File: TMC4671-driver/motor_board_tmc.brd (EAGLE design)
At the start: 60 x 110 mm, 163 parts, among them U1 TMC4671, U10 BSC030N08NS5ATMA1, U11 BSC030N08NS5ATMA1, U12 BSC030N08NS5ATMA1, U13 BSC030N08NS5ATMA1, U14 MCP14XX, U15 BSC030N08NS5ATMA1, U16 BSC030N08NS5ATMA1, U17 BSC030N08NS5ATMA1, U18 NC7NZ17K8X-3-BUFFER, U19 NC7NZ17K8X-3-BUFFER, U2 LM5109BSD, U20 LM74700-Q1, U22 BSC030N08NS5ATMA1, U23 MAX5033BASA+T, U24 AP3012KTR-G1, U3 LM5109BSD, U4 LM5109BSD, U5 LM5109BSD, U6 BSC030N08NS5ATMA1, U7 BSC030N08NS5ATMA1, U8 AD841X, U9 AD841X, X1 2516-, X2 GMSTBA4, X3 GMSTBA4, Y1 25MHz

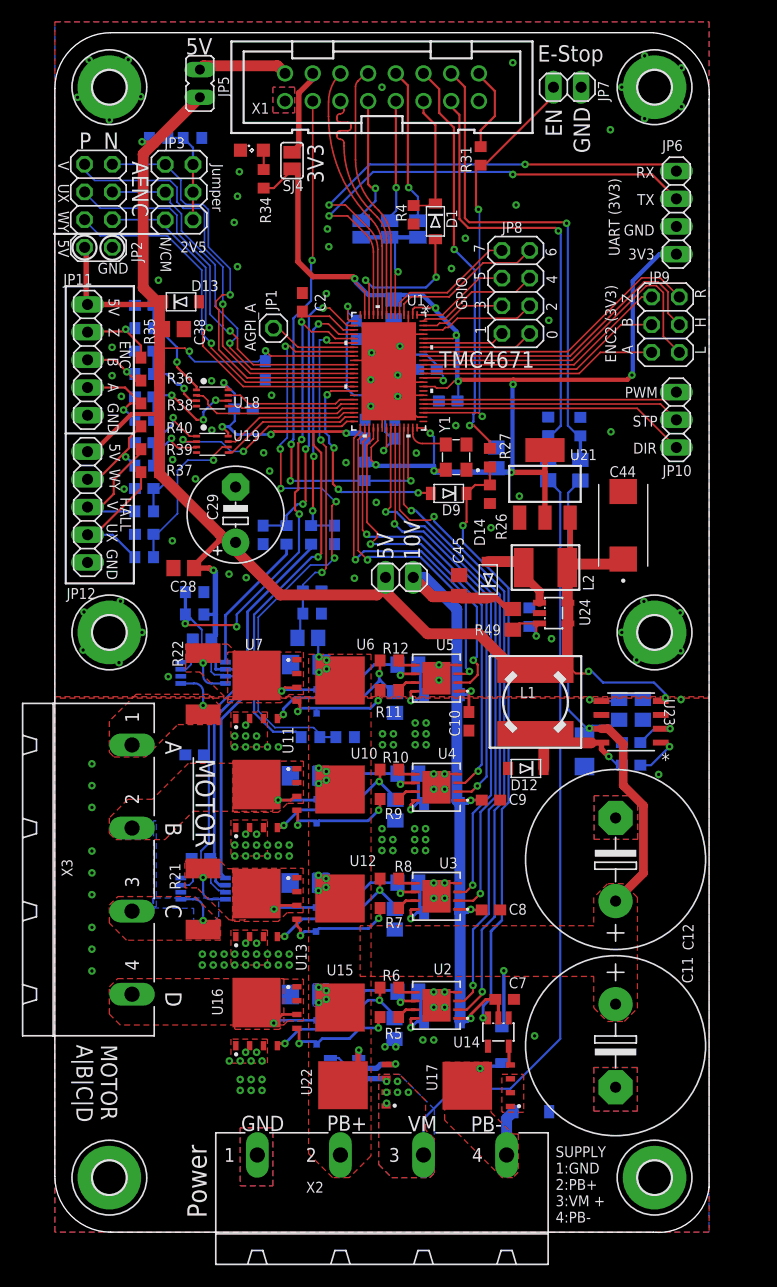
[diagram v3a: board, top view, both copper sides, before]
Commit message: Added E-Stop cap
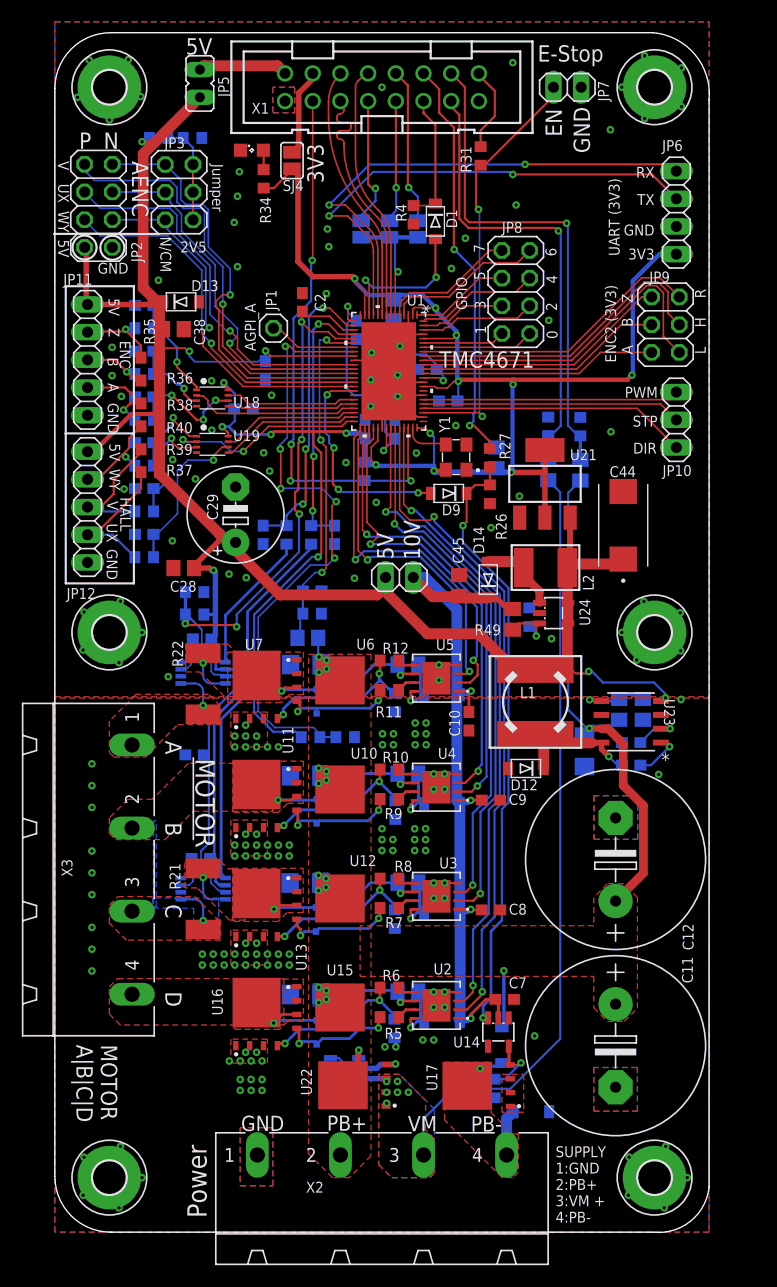
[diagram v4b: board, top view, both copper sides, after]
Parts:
- added R51: 33k, resistor:R0603
- C45: value 4.7µF -> 4.7µF <REMOVE>
- R17, R20, R25, R28: device resistor:R0805 -> resistor:R0603
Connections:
- net BRAKE_GATE: now also R51.2
- net GND: now also R51.1
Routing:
- net BRAKE_GATE: track 1.78 -> 5.88 mm, vias 0 -> 1
- net GND: vias 171 -> 181
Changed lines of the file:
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@@
 </element>
 <element name="D14" library="adafruit" library_urn="urn:adsk.eagle:library:420" package="SOD-123FL" package3d_urn="urn:adsk.eagle:package:6240937/1" value="LV low drop" x="39.75" y="-50.15" locked="yes" smashed="yes" rot="R90">
-<attribute name="NAME" x="39.45" y="-47.075" size="1" layer="25" font="vector" rot="R90"/>
+<attribute name="NAME" x="39.375" y="-47.8" size="1" layer="25" font="vector" rot="R90"/>
 <attribute name="VALUE" x="42.05" y="-51.25" size="1.27" layer="27" rot="R90"/>
 </element>
@@
 <attribute name="VALUE" x="45.43" y="-51.965" size="1" layer="28" rot="MR270"/>
 </element>
-<element name="C45" library="resistor" library_urn="urn:adsk.eagle:library:348" package="C0805" package3d_urn="urn:adsk.eagle:package:23617/2" value="4.7µF" x="37.075" y="-50.7" locked="yes" smashed="yes" rot="R90">
+<element name="C45" library="resistor" library_urn="urn:adsk.eagle:library:348" package="C0805" package3d_urn="urn:adsk.eagle:package:23617/2" value="4.7µF &lt;REMOVE&gt;" x="37.075" y="-50.7" locked="yes" smashed="yes" rot="R90">
 <attribute name="NAME" x="37.49" y="-48.685" size="1" layer="25" font="vector" rot="R90"/>
 <attribute name="VALUE" x="38.98" y="-51.335" size="1.27" layer="27" rot="R90"/>
@@
 <attribute name="VALUE" x="21.7" y="-92.775" size="1.27" layer="28" rot="MR90"/>
 </element>
-<element name="R17" library="resistor" library_urn="urn:adsk.eagle:library:348" package="R0805" package3d_urn="urn:adsk.eagle:package:23553/2" value="33k" x="31.2" y="-61.425" locked="yes" smashed="yes" rot="MR90">
+<element name="R17" library="resistor" library_urn="urn:adsk.eagle:library:348" package="R0603" package3d_urn="urn:adsk.eagle:package:23555/3" value="33k" x="31.2" y="-61.425" locked="yes" smashed="yes" rot="MR90">
 <attribute name="NAME" x="30.11" y="-60.58" size="1" layer="26" font="vector" rot="MR0"/>
 <attribute name="VALUE" x="28.66" y="-62.06" size="1.27" layer="28" rot="MR90"/>
 </element>
-<element name="R20" library="resistor" library_urn="urn:adsk.eagle:library:348" package="R0805" package3d_urn="urn:adsk.eagle:package:23553/2" value="33k" x="31.225" y="-71.3" locked="yes" smashed="yes" rot="MR90">
+<element name="R20" library="resistor" library_urn="urn:adsk.eagle:library:348" package="R0603" package3d_urn="urn:adsk.eagle:package:23555/3" value="33k" x="31.225" y="-71.3" locked="yes" smashed="yes" rot="MR90">
 <attribute name="NAME" x="30.285" y="-70.78" size="1" layer="26" font="vector" rot="MR0"/>
 <attribute name="VALUE" x="28.685" y="-71.935" size="1.27" layer="28" rot="MR90"/>
 </element>
-<element name="R25" library="resistor" library_urn="urn:adsk.eagle:library:348" package="R0805" package3d_urn="urn:adsk.eagle:package:23553/2" value="33k" x="31.175" y="-81.3" locked="yes" smashed="yes" rot="MR90">
+<element name="R25" library="resistor" library_urn="urn:adsk.eagle:library:348" package="R0603" package3d_urn="urn:adsk.eagle:package:23555/3" value="33k" x="31.175" y="-81.3" locked="yes" smashed="yes" rot="MR90">
 <attribute name="NAME" x="33.205" y="-82.04" size="1" layer="26" font="vector" rot="MR270"/>
 <attribute name="VALUE" x="28.635" y="-81.935" size="1.27" layer="28" rot="MR90"/>
 </element>
-<element name="R28" library="resistor" library_urn="urn:adsk.eagle:library:348" package="R0805" package3d_urn="urn:adsk.eagle:package:23553/2" value="33k" x="31.15" y="-91.325" locked="yes" smashed="yes" rot="MR90">
+<element name="R28" library="resistor" library_urn="urn:adsk.eagle:library:348" package="R0603" package3d_urn="urn:adsk.eagle:package:23555/3" value="33k" x="31.15" y="-91.325" locked="yes" smashed="yes" rot="MR90">
 <attribute name="NAME" x="33.005" y="-91.915" size="1" layer="26" font="vector" rot="MR270"/>
 <attribute name="VALUE" x="28.61" y="-91.96" size="1.27" layer="28" rot="MR90"/>
@@
 <attribute name="NAME" x="45.2" y="-97.825" size="1" layer="26" rot="MR0"/>
 <attribute name="VALUE" x="42.6" y="-97.666" size="0.4064" layer="28" rot="MR180"/>
+</element>
+<element name="R51" library="resistor" library_urn="urn:adsk.eagle:library:348" package="R0603" package3d_urn="urn:adsk.eagle:package:23555/3" value="33k" x="40.325" y="-96.825" smashed="yes" rot="MR90">
+<attribute name="NAME" x="41.595" y="-97.46" size="1.27" layer="26" rot="MR90"/>
+<attribute name="VALUE" x="37.785" y="-97.46" size="1.27" layer="28" rot="MR90"/>
 </element>
 </elements>
@@
 <via x="44" y="-92" extent="1-16" drill="0.3"/>
 <contactref element="D15" pad="A"/>
+<contactref element="R51" pad="1"/>
+<via x="58" y="-105" extent="1-16" drill="0.3"/>
+<via x="55.88375625" y="-107.772421875" extent="1-16" drill="0.3"/>
+<via x="52.593071875" y="-106.616484375" extent="1-16" drill="0.3"/>
+<via x="52.67555625" y="-103.12965" extent="1-16" drill="0.3"/>
+<via x="56.017221875" y="-102.13060625" extent="1-16" drill="0.3"/>
+<via x="8" y="-105" extent="1-16" drill="0.3"/>
+<via x="5.88375625" y="-107.772421875" extent="1-16" drill="0.3"/>
+<via x="2.593071875" y="-106.616484375" extent="1-16" drill="0.3"/>
+<via x="2.67555625" y="-103.12965" extent="1-16" drill="0.3"/>
+<via x="6.017221875" y="-102.13060625" extent="1-16" drill="0.3"/>
 </signal>
 <signal name="G_LS_D">
@@
 <wire x1="31.15" y1="-90.375" x2="31.15" y2="-90.1084" width="0.254" layer="16"/>
 <wire x1="31.15" y1="-90.1084" x2="29.775" y2="-88.7334" width="0.254" layer="16"/>
+<wire x1="31.15" y1="-90.375" x2="31.15" y2="-90.475" width="0" layer="19" extent="16-16"/>
 </signal>
 <signal name="MOT_C">
@@
 <wire x1="31.175" y1="-80.35" x2="31.175" y2="-80.0084" width="0.254" layer="16"/>
 <wire x1="31.175" y1="-80.0084" x2="29.8" y2="-78.6334" width="0.254" layer="16"/>
+<wire x1="31.175" y1="-80.35" x2="31.175" y2="-80.45" width="0" layer="19" extent="16-16"/>
 </signal>
 <signal name="G_HS_C">
@@
 <wire x1="31.2" y1="-60.475" x2="30.925" y2="-60.475" width="0.254" layer="16"/>
 <wire x1="30.925" y1="-60.475" x2="29.825" y2="-59.375" width="0.254" layer="16"/>
+<wire x1="31.2" y1="-60.475" x2="31.2" y2="-60.575" width="0" layer="19" extent="16-16"/>
 </signal>
 <signal name="G_LS_B">
@@
 <wire x1="29.75" y1="-68.675" x2="31.225" y2="-70.15" width="0.254" layer="16"/>
 <wire x1="31.225" y1="-70.15" x2="31.225" y2="-70.35" width="0.254" layer="16"/>
+<wire x1="31.225" y1="-70.35" x2="31.225" y2="-70.45" width="0" layer="19" extent="16-16"/>
 </signal>
 <signal name="INPUT_GATE">
@@
 <wire x1="41.775" y1="-94.67" x2="41.65" y2="-94.545" width="0.3" layer="1"/>
 <wire x1="41.625" y1="-92.95" x2="41.65" y2="-92.975" width="0.3" layer="1"/>
+<contactref element="R51" pad="2"/>
+<wire x1="40.325" y1="-95.975" x2="41.25" y2="-95.975" width="0.2" layer="16"/>
+<wire x1="41.25" y1="-95.975" x2="42.75" y2="-94.475" width="0.2" layer="16"/>
+<via x="42.75" y="-94.475" extent="1-16" drill="0.3"/>
+<wire x1="42.75" y1="-94.475" x2="42.555" y2="-94.67" width="0.2" layer="1"/>
+<wire x1="42.555" y1="-94.67" x2="41.775" y2="-94.67" width="0.2" layer="1"/>
 </signal>
 <signal name="V_SENSE/2">

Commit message: Fixed tmc silkscreen (Resistor names, labels)
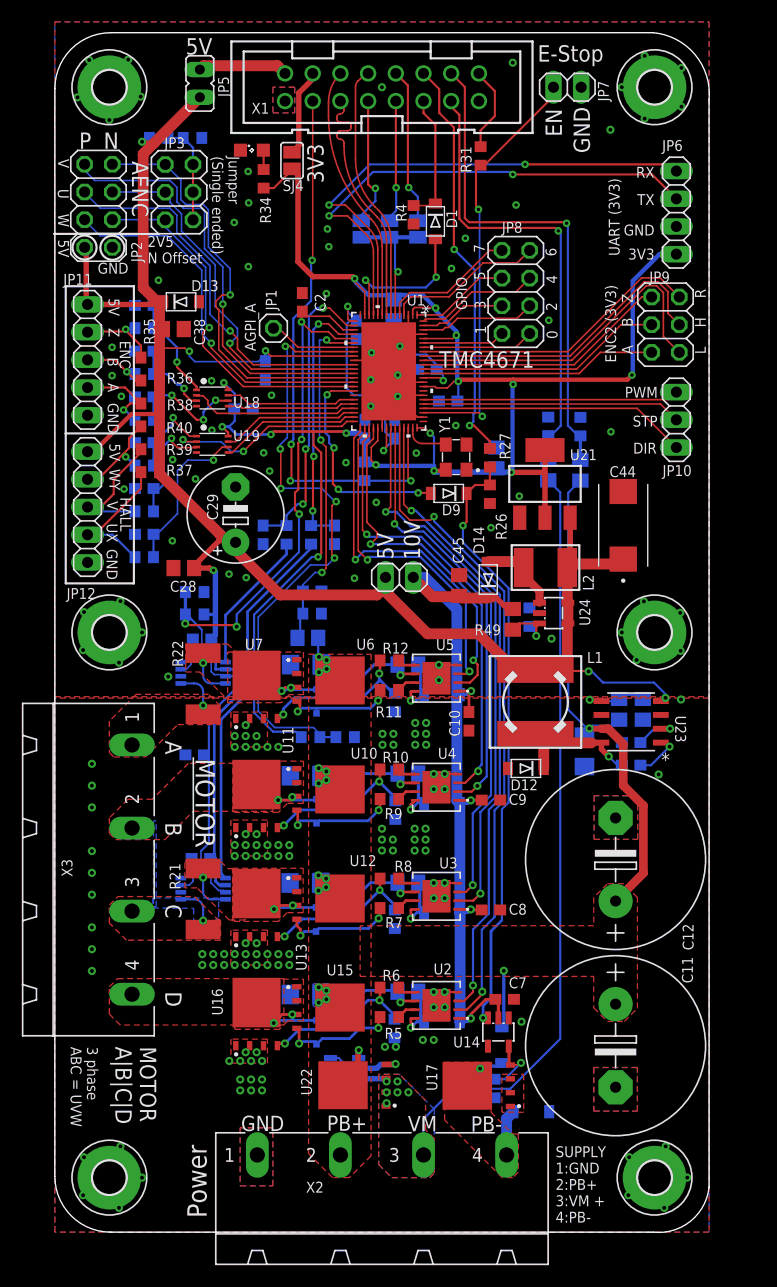
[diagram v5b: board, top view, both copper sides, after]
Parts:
- D15: value Zener 65V -> Zener 65V (MMSZ5265BT1G)
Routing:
- net MOT_D: track 17.6 -> 18.2 mm, vias 2 -> 3
- net G_LS_A: track 14.9 -> 15.5 mm
- net G_LS_B: track 14.5 -> 15.1 mm
- net MOT_B: track 16.3 -> 16.8 mm, vias 2 -> 3
- net MOT_A: track 20.0 -> 20.5 mm, vias 3 -> 4
- net MOT_C: track 21.5 -> 21.8 mm, vias 3 -> 4
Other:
- board text added: "2V5 N Offset"
- board text added: "3 phase ABC = UVW"
- board text added: "Jumper (Single ended)"
- board text added: "N Offset"
- board text added: "STEPPER: AB(A) CD(B) | 3 PHASE: ABC(UVW) | DC: AB"
- board text added: "Supply: PSU (protected): VM (+) and GND (-) ALWAYS use braking resistor between PB+ and PB Battery: PB+ (+) and GND (-) No resistor"
- board text added: "U"
- board text added: "V1.2.1 - YR 2021"
- board text added: "W"
- board text removed: "Jumper"
- board text removed: "SE Select"
- board text removed: "STEPPER: AB CD | 3 PHASE: ABC | DC: AB"
- board text removed: "Supply: PSU (protected): use VM (+) and GND (-) ALWAYS use braking resistor between PB+ and PB Battery (unprotected. regen. braking): Only PB+ (+) and GND (-)"
- board text removed: "V1.2 - YR 2020"
